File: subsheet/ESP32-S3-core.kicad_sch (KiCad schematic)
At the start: 22 parts, among them Q601 40MHz, U301 W25Q128JVS, U302 ESP32-S3R8

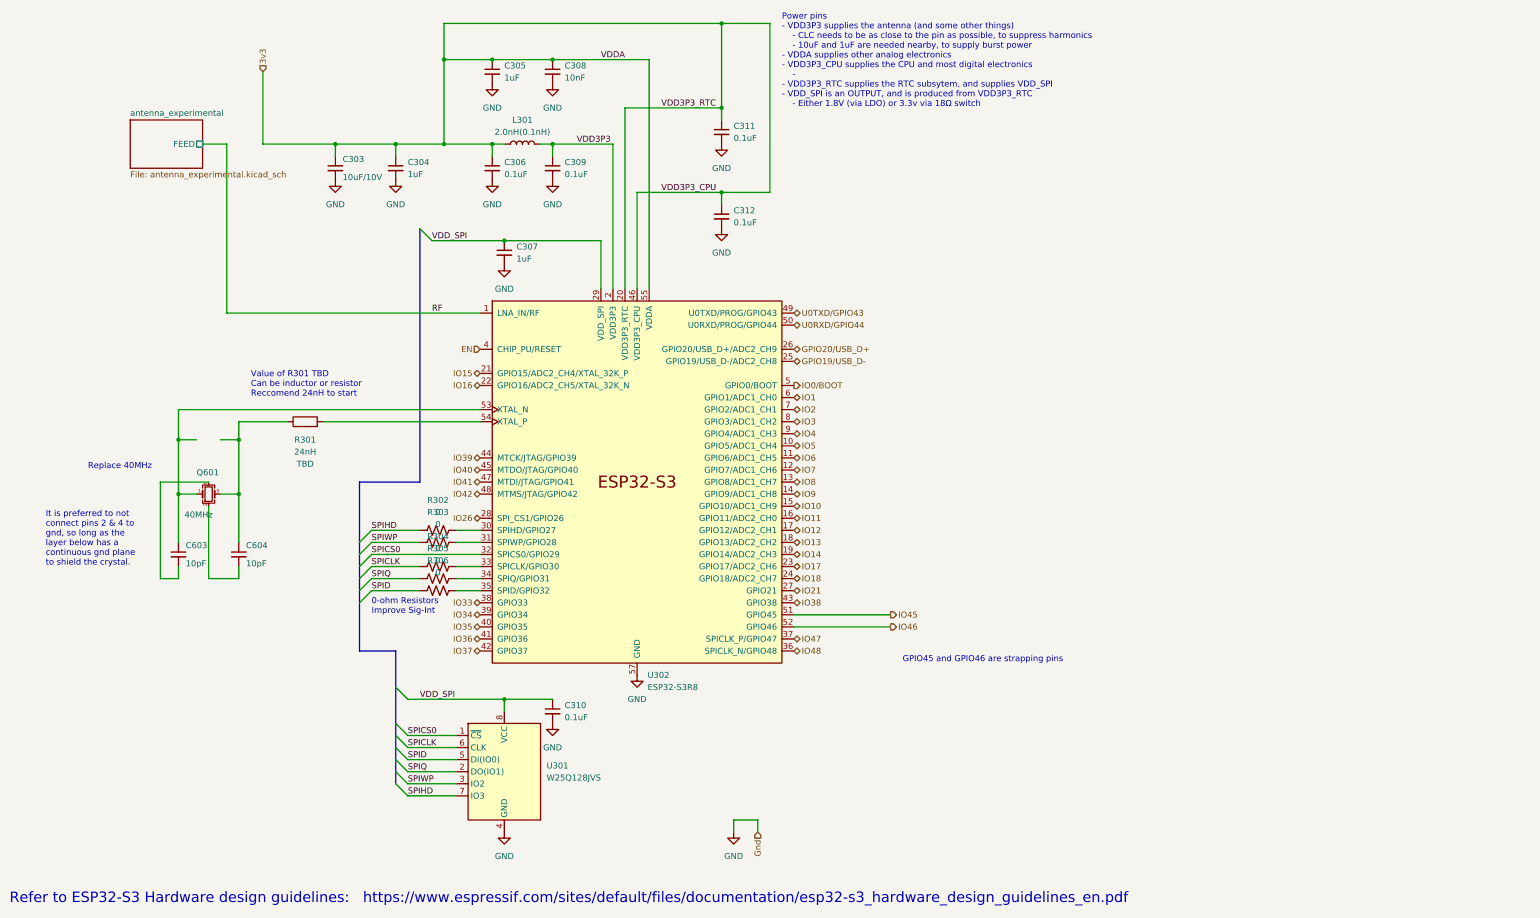
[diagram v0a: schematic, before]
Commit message: Move all subsheets into 'main' subsheet, below root
Keeping all the subsheets in a dedicated 'subsheet' folder makes things
much, much neater. However, specifying filepaths for subsheets has an
interesting problem; they use paths RELATIVE TO THE PARENT SHEET.

The consequence of is that if a subsheet is part of the root sheet, it
needs to be prefixed with 'subsheet/', but NOT if it's further down.
This inconsistency can be resolved by having a single 'main' sheet at
the top that doesn't move.

It's also useful to have a top-level space to put down changelogs,
descriptions etc.
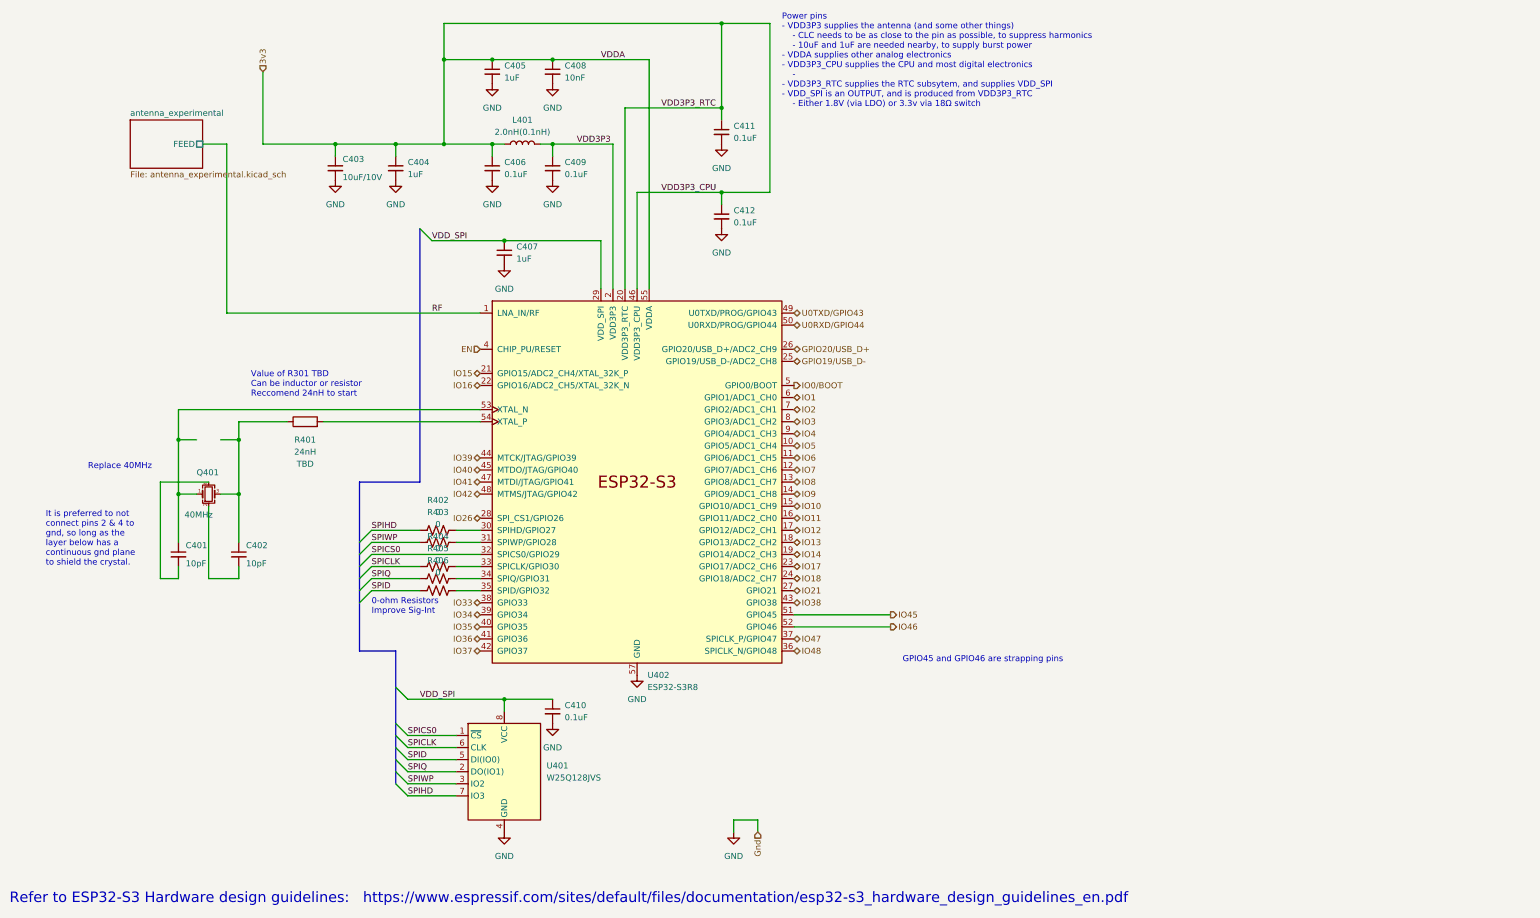
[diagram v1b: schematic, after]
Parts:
- renumbered C603 to C401, C604 to C402, C303 to C403, C304 to C404, C305 to C405, C306 to C406, C307 to C407, C308 to C408, C309 to C409, C310 to C410, C311 to C411, C312 to C412, L301 to L401, Q601 to Q401, R301 to R401, R302 to R402, R303 to R403, R304 to R404, R305 to R405, R306 to R406, U301 to U401, U302 to U402

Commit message: Update file format to KiCAD 9.0
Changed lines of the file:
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@@
 (kicad_sch
-	(version 20231120)
+	(version 20250114)
 	(generator "eeschema")
-	(generator_version "8.0")
+	(generator_version "9.0")
 	(paper "A4")
 	(title_block
@@
 		(company "(c) Vincent Dalstra")
 	)
+	(text "0-ohm Resistors\nImprove Sig-Int"
+		(exclude_from_sim no)
+		(at 88.9 144.78 0)
+		(effects
+			(font
+				(size 1.27 1.27)
+			)
+			(justify left bottom)
+		)
+	)
+	(text "Value of R301 TBD\nCan be inductor or resistor\nReccomend 24nH to start"
+		(exclude_from_sim no)
+		(at 63.5 99.06 0)
+		(effects
+			(font
+				(size 1.27 1.27)
+			)
+			(justify left bottom)
+		)
+	)
+	(text "Power pins\n- VDD3P3 supplies the antenna (and some other things)\n	- CLC needs to be as close to the pin as possible, to suppress harmonics\n	- 10uF and 1uF are needed nearby, to supply burst power\n- VDDA supplies other analog electronics\n- VDD3P3_CPU supplies the CPU and most digital electronics\n	- \n- VDD3P3_RTC supplies the RTC subsytem, and supplies VDD_SPI\n- VDD_SPI is an OUTPUT, and is produced from VDD3P3_RTC\n	- Either 1.8V (via LDO) or 3.3v via 18Ω switch"
+		(exclude_from_sim no)
+		(at 175.26 38.1 0)
+		(effects
+			(font
+				(size 1.27 1.27)
+			)
+			(justify left bottom)
+		)
+	)
+	(text "It is preferred to not\nconnect pins 2 & 4 to\ngnd, so long as the\nlayer below has a\ncontinuous gnd plane\nto shield the crystal."
+		(exclude_from_sim no)
+		(at 20.32 134.62 0)
+		(effects
+			(font
+				(size 1.27 1.27)
+			)
+			(justify left bottom)
+		)
+	)
+	(text "Refer to ESP32-S3 Hardware design guidelines:   https://www.espressif.com/sites/default/files/documentation/esp32-s3_hardware_design_guidelines_en.pdf"
+		(exclude_from_sim no)
+		(at 12.7 205.74 0)
+		(effects
+			(font
+				(size 2.2 2.2)
+			)
+			(justify left bottom)
+		)
+	)
+	(text "GPIO45 and GPIO46 are strapping pins"
+		(exclude_from_sim no)
+		(at 200.66 154.94 0)
+		(effects
+			(font
+				(size 1.27 1.27)
+			)
+			(justify left bottom)
+		)
+	)
+	(text "Replace 40MHz"
+		(exclude_from_sim no)
+		(at 29.21 114.3 0)
+		(effects
+			(font
+				(size 1.27 1.27)
+			)
+			(justify left bottom)
+		)
+	)
 	(junction
 		(at 162.56 55.88)
@@
 		)
 	)
-	(text "0-ohm Resistors\nImprove Sig-Int"
-		(exclude_from_sim no)
-		(at 88.9 144.78 0)
-		(effects
-			(font
-				(size 1.27 1.27)
-			)
-			(justify left bottom)
-		)
-	)
-	(text "Value of R301 TBD\nCan be inductor or resistor\nReccomend 24nH to start"
-		(exclude_from_sim no)
-		(at 63.5 99.06 0)
-		(effects
-			(font
-				(size 1.27 1.27)
-			)
-			(justify left bottom)
-		)
-	)
-	(text "Power pins\n- VDD3P3 supplies the antenna (and some other things)\n	- CLC needs to be as close to the pin as possible, to suppress harmonics\n	- 10uF and 1uF are needed nearby, to supply burst power\n- VDDA supplies other analog electronics\n- VDD3P3_CPU supplies the CPU and most digital electronics\n	- \n- VDD3P3_RTC supplies the RTC subsytem, and supplies VDD_SPI\n- VDD_SPI is an OUTPUT, and is produced from VDD3P3_RTC\n	- Either 1.8V (via LDO) or 3.3v via 18Ω switch"
-		(exclude_from_sim no)
-		(at 175.26 38.1 0)
-		(effects
-			(font
-				(size 1.27 1.27)
-			)
-			(justify left bottom)
-		)
-	)
-	(text "It is preferred to not\nconnect pins 2 & 4 to\ngnd, so long as the\nlayer below has a\ncontinuous gnd plane\nto shield the crystal."
-		(exclude_from_sim no)
-		(at 20.32 134.62 0)
-		(effects
-			(font
-				(size 1.27 1.27)
-			)
-			(justify left bottom)
-		)
-	)
-	(text "Refer to ESP32-S3 Hardware design guidelines:   https://www.espressif.com/sites/default/files/documentation/esp32-s3_hardware_design_guidelines_en.pdf"
-		(exclude_from_sim no)
-		(at 12.7 205.74 0)
-		(effects
-			(font
-				(size 2.2 2.2)
-			)
-			(justify left bottom)
-		)
-	)
-	(text "GPIO45 and GPIO46 are strapping pins"
-		(exclude_from_sim no)
-		(at 200.66 154.94 0)
-		(effects
-			(font
-				(size 1.27 1.27)
-			)
-			(justify left bottom)
-		)
-	)
-	(text "Replace 40MHz"
-		(exclude_from_sim no)
-		(at 29.21 114.3 0)
-		(effects
-			(font
-				(size 1.27 1.27)
-			)
-			(justify left bottom)
-		)
-	)
 	(label "SPIWP"
 		(at 96.52 180.34 0)
@@
 		(at 38.1 40.64)
 		(size 15.24 10.16)
+		(exclude_from_sim no)
+		(in_bom yes)
+		(on_board yes)
+		(dnp no)
 		(fields_autoplaced yes)
 		(stroke
